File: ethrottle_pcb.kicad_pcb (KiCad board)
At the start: 2 copper layers, 50 parts, among them J1 ATM15-08PA-BM02, K1 1462042-9, U1 LM4040DBZ-5, U2 LM324, U3 LM358_DFN, U4 LM324

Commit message: routes
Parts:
- moved J1 59.0 mm to (141.2, 77.9)
- moved U3 1.13 mm to (114.2, 77.7)
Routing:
- net GND: track 23.2 -> 84.4 mm, vias 20 -> 22
- net Net-(R15-Pad1): track 0.00 -> 9.18 mm
- net Net-(D15-Pad1): track 0.00 -> 5.23 mm
- net 4.5V: track 0.08 -> 4.65 mm
- net Net-(D7-Pad2): track 5.78 -> 9.42 mm
- net Net-(D8-Pad2): track 0.00 -> 2.83 mm
- net Net-(D13-Pad1): track 0.00 -> 2.75 mm
- net Net-(D14-Pad2): track 0.00 -> 2.74 mm
- net Brake: track 0.00 -> 2.10 mm
- net Net-(D2-Pad2): track 0.00 -> 1.80 mm
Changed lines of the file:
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@@
   )
   (footprint "Package_DFN_QFN:DFN-8-1EP_2x2mm_P0.5mm_EP1.05x1.75mm" (layer "F.Cu")
-    (at 115.316 77.6685)
+    (at 114.184 77.736)
     (descr "DFN8 2x2, 0.5P; CASE 506CN (see ON Semiconductor 506CN.PDF)")
     (tags "DFN 0.5")
@@
   )
   (footprint "ATM15-08PA-BM02:ATM1508PABM02" (layer "B.Cu")
-    (at 82.262 79.708 90)
+    (at 141.218 77.928 90)
     (descr "ATM15-08PA-BM02-2")
     (tags "Connector")
@@
   (segment (start 122.936 76.456) (end 120.396 76.456) (width 0.127) (layer "F.Cu") (net 1))
   (segment (start 105.718 82.17) (end 105.718 81.212) (width 0.127) (layer "F.Cu") (net 1))
+  (segment (start 141.218 65.328) (end 140.004 65.328) (width 0.127) (layer "F.Cu") (net 2))
   (segment (start 106.16 83.694) (end 107.496 83.694) (width 0.127) (layer "F.Cu") (net 2))
   (segment (start 102.34 52.054) (end 100.854 52.054) (width 0.127) (layer "F.Cu") (net 2))
@@
   (segment (start 108.208 56.134) (end 108.208 55.63) (width 0.127) (layer "F.Cu") (net 2))
   (segment (start 112.268 81.916) (end 111.506 81.916) (width 0.127) (layer "F.Cu") (net 2))
-  (segment (start 113.3425 78.4185) (end 113.284 78.36) (width 0.127) (layer "F.Cu") (net 2))
+  (segment (start 112.2105 78.486) (end 112.152 78.4275) (width 0.127) (layer "F.Cu") (net 2))
   (segment (start 116.815 58.164) (end 116.84 58.189) (width 0.127) (layer "F.Cu") (net 2))
   (segment (start 109.96 52.054) (end 108.474 52.054) (width 0.127) (layer "F.Cu") (net 2))
   (segment (start 114.554 56.919) (end 115.062 57.427) (width 0.127) (layer "F.Cu") (net 2))
+  (segment (start 140.004 65.328) (end 139.7 65.024) (width 0.127) (layer "F.Cu") (net 2))
   (segment (start 105.156 69.6214) (end 105.156 68.072) (width 0.127) (layer "F.Cu") (net 2))
   (segment (start 111.51 76.2) (end 111.51 76.958) (width 0.127) (layer "F.Cu") (net 2))
   (segment (start 114.554 56.388) (end 114.554 56.919) (width 0.127) (layer "F.Cu") (net 2))
+  (segment (start 129.4065 63.8745) (end 129.54 64.008) (width 0.127) (layer "F.Cu") (net 2))
   (segment (start 116.078 55.395) (end 116.078 54.379) (width 0.127) (layer "F.Cu") (net 2))
   (segment (start 118.872 83.186) (end 119.38 83.694) (width 0.127) (layer "F.Cu") (net 2))
@@
   (segment (start 100.276 68.3744) (end 101.2976 68.3744) (width 0.127) (layer "F.Cu") (net 2))
   (segment (start 100.854 52.054) (end 100.838 52.07) (width 0.127) (layer "F.Cu") (net 2))
+  (segment (start 127.5715 63.8745) (end 129.4065 63.8745) (width 0.127) (layer "F.Cu") (net 2))
   (segment (start 108.474 52.054) (end 108.458 52.07) (width 0.127) (layer "F.Cu") (net 2))
   (segment (start 111.8235 69.39915) (end 111.8235 67.6275) (width 0.127) (layer "F.Cu") (net 2))
-  (segment (start 114.416 78.4185) (end 113.3425 78.4185) (width 0.127) (layer "F.Cu") (net 2))
+  (segment (start 113.284 78.486) (end 112.2105 78.486) (width 0.127) (layer "F.Cu") (net 2))
   (segment (start 111.51 76.958) (end 111.506 76.962) (width 0.127) (layer "F.Cu") (net 2))
   (segment (start 116.078 58.164) (end 116.815 58.164) (width 0.127) (layer "F.Cu") (net 2))
@@
   (via (at 124.206 49.022) (size 0.4) (drill 0.2) (layers "F.Cu" "B.Cu") (net 2))
   (via (at 119.38 83.694) (size 0.4) (drill 0.2) (layers "F.Cu" "B.Cu") (net 2))
-  (via (at 113.284 78.36) (size 0.4) (drill 0.2) (layers "F.Cu" "B.Cu") (net 2))
+  (via (at 112.152 78.4275) (size 0.4) (drill 0.2) (layers "F.Cu" "B.Cu") (net 2))
   (via (at 108.458 52.07) (size 0.4) (drill 0.2) (layers "F.Cu" "B.Cu") (net 2))
+  (via (at 139.7 65.024) (size 0.4) (drill 0.2) (layers "F.Cu" "B.Cu") (net 2))
   (via (at 107.496 83.694) (size 0.4) (drill 0.2) (layers "F.Cu" "B.Cu") (net 2))
   (via (at 112.014 55.88) (size 0.4) (drill 0.2) (layers "F.Cu" "B.Cu") (net 2))
   (via (at 108.989 76.328) (size 0.4) (drill 0.2) (layers "F.Cu" "B.Cu") (net 2))
+  (via (at 129.54 64.008) (size 0.4) (drill 0.2) (layers "F.Cu" "B.Cu") (net 2))
   (via (at 111.506 76.962) (size 0.4) (drill 0.2) (layers "F.Cu" "B.Cu") (net 2))
   (via (at 115.062 81.408) (size 0.4) (drill 0.2) (layers "F.Cu" "B.Cu") (net 2))
@@
   (via (at 105.156 68.072) (size 0.4) (drill 0.2) (layers "F.Cu" "B.Cu") (net 2))
   (via (at 108.204 55.626) (size 0.4) (drill 0.2) (layers "F.Cu" "B.Cu") (net 2))
+  (segment (start 148.618 58.418) (end 130.304 58.418) (width 0.127) (layer "B.Cu") (net 2))
+  (segment (start 126.718 58.418) (end 130.3 58.418) (width 0.127) (layer "B.Cu") (net 2))
+  (segment (start 130.302 58.42) (end 130.302 63.246) (width 0.127) (layer "B.Cu") (net 2))
+  (segment (start 130.3 58.418) (end 130.302 58.42) (width 0.127) (layer "B.Cu") (net 2))
+  (segment (start 126.718 84.838) (end 120.524 84.838) (width 0.127) (layer "B.Cu") (net 2))
+  (segment (start 130.302 63.246) (end 129.54 64.008) (width 0.127) (layer "B.Cu") (net 2))
+  (segment (start 120.524 84.838) (end 119.38 83.694) (width 0.127) (layer "B.Cu") (net 2))
+  (segment (start 148.618 84.838) (end 126.718 84.838) (width 0.127) (layer "B.Cu") (net 2))
+  (segment (start 130.304 58.418) (end 130.302 58.42) (width 0.127) (layer "B.Cu") (net 2))
   (segment (start 116.52 52.888) (end 116.59 52.958) (width 0.127) (layer "F.Cu") (net 3))
+  (segment (start 114.554 55.418) (end 114.554 53.613) (width 0.127) (layer "F.Cu") (net 5))
   (segment (start 100.276 69.3444) (end 100.276 73.602) (width 0.127) (layer "F.Cu") (net 6))
   (segment (start 100.276 73.602) (end 100.334 73.66) (width 0.127) (layer "F.Cu") (net 6))
@@
   (segment (start 120.142 81.916) (end 120.65 81.916) (width 0.127) (layer "B.Cu") (net 8))
   (segment (start 121.666 82.932) (end 122.682 82.932) (width 0.127) (layer "B.Cu") (net 8))
+  (segment (start 106.934 75.694) (end 108.865 75.694) (width 0.127) (layer "F.Cu") (net 9))
+  (segment (start 108.865 75.694) (end 109.501 75.058) (width 0.127) (layer "F.Cu") (net 9))
   (segment (start 122.682 82.428) (end 122.936 82.174) (width 0.127) (layer "F.Cu") (net 10))
   (segment (start 122.936 82.174) (end 122.936 79.756) (width 0.127) (layer "F.Cu") (net 10))
   (segment (start 103.205999 70.276001) (end 103.205999 68.8594) (width 0.127) (layer "F.Cu") (net 13))
+  (segment (start 102.868 75.694) (end 103.632 75.694) (width 0.127) (layer "F.Cu") (net 13))
   (segment (start 100.834 72.648) (end 103.205999 70.276001) (width 0.127) (layer "F.Cu") (net 13))
   (segment (start 100.834 73.66) (end 100.834 72.648) (width 0.127) (layer "F.Cu") (net 13))
+  (segment (start 100.834 73.66) (end 102.868 75.694) (width 0.127) (layer "F.Cu") (net 13))
   (segment (start 105.16 81.078526) (end 105.16 81.154) (width 0.127) (layer "F.Cu") (net 16))
   (segment (start 106.934 79.938) (end 106.734 80.138) (width 0.127) (layer "F.Cu") (net 16))
@@
   (segment (start 106.934 78.994) (end 106.934 79.938) (width 0.127) (layer "F.Cu") (net 16))
   (segment (start 103.632 79.626) (end 105.16 81.154) (width 0.127) (layer "F.Cu") (net 16))
+  (segment (start 112.01 76.2) (end 112.01 76.704) (width 0.127) (layer "F.Cu") (net 17))
+  (segment (start 112.01 76.704) (end 112.792 77.486) (width 0.127) (layer "F.Cu") (net 17))
+  (segment (start 112.792 77.486) (end 113.284 77.486) (width 0.127) (layer "F.Cu") (net 17))
   (segment (start 120.646 80.006) (end 120.396 79.756) (width 0.127) (layer "F.Cu") (net 19))
   (segment (start 120.646 83.186) (end 120.646 80.006) (width 0.127) (layer "F.Cu") (net 19))
   (segment (start 117.09 52.582) (end 119.126 50.546) (width 0.127) (layer "F.Cu") (net 20))
   (segment (start 117.09 52.958) (end 117.09 52.582) (width 0.127) (layer "F.Cu") (net 20))
+  (segment (start 113.156 69.43165) (end 113.1235 69.39915) (width 0.127) (layer "F.Cu") (net 21))
+  (segment (start 113.156 72.136) (end 113.156 69.43165) (width 0.127) (layer "F.Cu") (net 21))
+  (segment (start 117.263 72.852) (end 120.8405 69.2745) (width 0.127) (layer "F.Cu") (net 23))
+  (segment (start 117.094 72.852) (end 117.263 72.852) (width 0.127) (layer "F.Cu") (net 23))
   (segment (start 110.036 75.093) (end 110.036 77.598) (width 0.127) (layer "F.Cu") (net 26))
   (segment (start 110.001 75.058) (end 110.036 75.093) (width 0.127) (layer "F.Cu") (net 26))
+  (segment (start 102.566 73.456) (end 103.856 72.166) (width 0.127) (layer "F.Cu") (net 27))
   (segment (start 102.566 73.66) (end 102.566 73.735474) (width 0.127) (layer "F.Cu") (net 27))
+  (segment (start 102.566 73.66) (end 102.566 73.456) (width 0.127) (layer "F.Cu") (net 27))
+  (segment (start 103.856 72.166) (end 103.856 69.6214) (width 0.127) (layer "F.Cu") (net 27))
   (segment (start 116.5856 70.081) (end 116.611 70.1064) (width 0.127) (layer "F.Cu") (net 28))
   (segment (start 119.126 55.88) (end 119.126 53.846) (width 0.127) (layer "F.Cu") (net 30))
+  (segment (start 109.873499 69.39915) (end 109.873499 72.118501) (width 0.127) (layer "F.Cu") (net 32))
+  (segment (start 109.873499 72.118501) (end 109.856 72.136) (width 0.127) (layer "F.Cu") (net 32))
   (segment (start 117.111 70.1064) (end 117.111 71.865) (width 0.127) (layer "F.Cu") (net 33))
   (segment (start 117.111 71.865) (end 117.094 71.882) (width 0.127) (layer "F.Cu") (net 33))
+  (segment (start 103.206001 63.9826) (end 100.609 61.385599) (width 0.127) (layer "F.Cu") (net 35))
+  (segment (start 100.609 61.385599) (end 100.609 55.88) (width 0.127) (layer "F.Cu") (net 35))
   (zone (net 28) (net_name "+12V") (layer "F.Cu") (name "12V") (hatch edge 0.508)
     (priority 2)

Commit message: update constraints
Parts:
- moved U4 22.8 mm to (128.8, 51.3)
- moved J1 22.6 mm to (118.6, 78.9)
- moved D14 18.6 mm to (129.3, 77.7), turned to 90 degrees
- moved R13 11.0 mm to (111.8, 81.5)
- moved D5 8.36 mm to (109.5, 83.3)
- moved R12 8.36 mm to (112.0, 83.3)
- moved R3 5.67 mm to (114.2, 81.3)
- moved U3 5.67 mm to (116.6, 82.9)
- moved R4 5.34 mm to (110.0, 80.5)
- moved C1 4.94 mm to (101.1, 81.0), turned to -90 degrees
- moved D4 4.83 mm to (106.1, 74.2)
- moved D6 4.83 mm to (107.9, 81.8)
- moved R11 3.71 mm to (106.9, 72.6), turned to 180 degrees
- moved D9 3.07 mm to (123.4, 77.7)
- moved D10 3.07 mm to (126.0, 77.7)
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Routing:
- net GND: track 84.4 -> 40.5 mm, vias 22 -> 16
- net Brake: track 2.10 -> 18.9 mm, vias 0 -> 1
- net Throttle: track 0.00 -> 13.7 mm, vias 0 -> 2
- net 0.5V: track 0.00 -> 11.0 mm
- net Net-(R25-Pad2): track 0.00 -> 7.37 mm
- net Net-(D10-Pad2): track 2.78 -> 9.84 mm
- net Net-(D6-Pad2): track 9.86 -> 3.35 mm, vias 1 -> 0
- net Net-(D7-Pad2): track 9.42 -> 5.02 mm
- net Net-(D9-Pad2): track 3.53 -> 0.00 mm
- net Net-(C1-Pad1): track 5.71 -> 2.54 mm
- net Net-(D8-Pad2): track 2.83 -> 0.00 mm
- net Net-(D13-Pad1): track 2.75 -> 0.00 mm
- net Net-(D14-Pad2): track 2.74 -> 0.00 mm
- net Net-(D15-Pad1): track 5.23 -> 6.88 mm
- net +5V: track 0.00 -> 1.56 mm
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
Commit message: more traces
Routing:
- net Net-(D13-Pad1): track 0.00 -> 37.4 mm, vias 0 -> 4
- net 0.5V: track 11.0 -> 41.5 mm, vias 0 -> 4
- net Net-(C1-Pad1): track 2.54 -> 28.4 mm, vias 0 -> 2
- net Net-(D14-Pad2): track 0.00 -> 25.6 mm
- net 4.5V: track 4.60 -> 27.0 mm, vias 0 -> 3
- net BREF: track 0.00 -> 22.2 mm
- net Net-(C2-Pad1): track 0.00 -> 21.1 mm, vias 0 -> 3
- net Net-(K1-Pad1): track 0.00 -> 17.9 mm, vias 0 -> 2
- net Brake: track 18.9 -> 33.0 mm, vias 1 -> 2
- net Net-(D9-Pad2): track 0.00 -> 12.9 mm
- net Net-(D12-Pad2): track 2.03 -> 12.2 mm
- net Net-(D8-Pad2): track 0.00 -> 6.63 mm
- net Net-(D7-Pad2): track 5.02 -> 8.66 mm
- net GND: track 40.5 -> 42.3 mm, vias 16 -> 17

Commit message: more traces
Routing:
- net +12V: track 0.00 -> 79.6 mm, vias 0 -> 8
- net Net-(D1-Pad2): track 0.00 -> 42.8 mm, vias 0 -> 6
- net Net-(R14-Pad2): track 0.00 -> 42.6 mm, vias 0 -> 2
- net Net-(R18-Pad2): track 0.00 -> 40.4 mm, vias 0 -> 2
- net 4.5V: track 27.0 -> 65.0 mm, vias 3 -> 5
- net Throttle: track 13.7 -> 51.5 mm, vias 2 -> 5
- net Net-(C1-Pad1): track 28.4 -> 65.9 mm, vias 2 -> 4
- net Net-(R15-Pad1): track 9.18 -> 37.8 mm, vias 0 -> 4
- net Net-(D10-Pad2): track 9.84 -> 27.7 mm
- net Brake: track 33.0 -> 49.4 mm, vias 2 -> 3
- net +5V: track 1.58 -> 15.5 mm, vias 0 -> 4
- net Net-(C2-Pad1): track 21.1 -> 33.2 mm
- net Net-(R14-Pad1): track 1.22 -> 12.9 mm
- net Net-(D14-Pad2): track 25.6 -> 29.4 mm
- net GND: track 42.3 -> 40.7 mm, vias 17 -> 16
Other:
- board outline added: 36.8 x 54.6 mm

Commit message: more traces
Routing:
- net TREF: track 0.00 -> 22.8 mm, vias 0 -> 2
- net GND: track 40.7 -> 54.7 mm, vias 16 -> 18
- net Throttle: track 51.5 -> 58.8 mm, vias 5 -> 7
- net 0.5V: track 41.5 -> 47.3 mm
- net Brake: track 49.4 -> 54.0 mm, vias 3 -> 4
- net 4.5V: track 65.0 -> 68.4 mm

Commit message: 0 unconnected
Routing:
- net Net-(R25-Pad2): track 7.37 -> 76.2 mm, vias 0 -> 4
- net GND: track 54.7 -> 100.2 mm, vias 18 -> 24
- net Net-(R23-Pad1): track 0.00 -> 34.4 mm, vias 0 -> 6
- net +5V: track 15.5 -> 45.6 mm, vias 4 -> 8
- net Net-(D13-Pad1): track 37.4 -> 38.6 mm
- net +12V: track 79.6 -> 78.4 mm
- net 4.5V: track 68.4 -> 69.4 mm
- net Net-(C2-Pad1): track 33.2 -> 34.0 mm
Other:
- board size 36.8 x 54.6 mm -> 37.7 x 55.9 mm

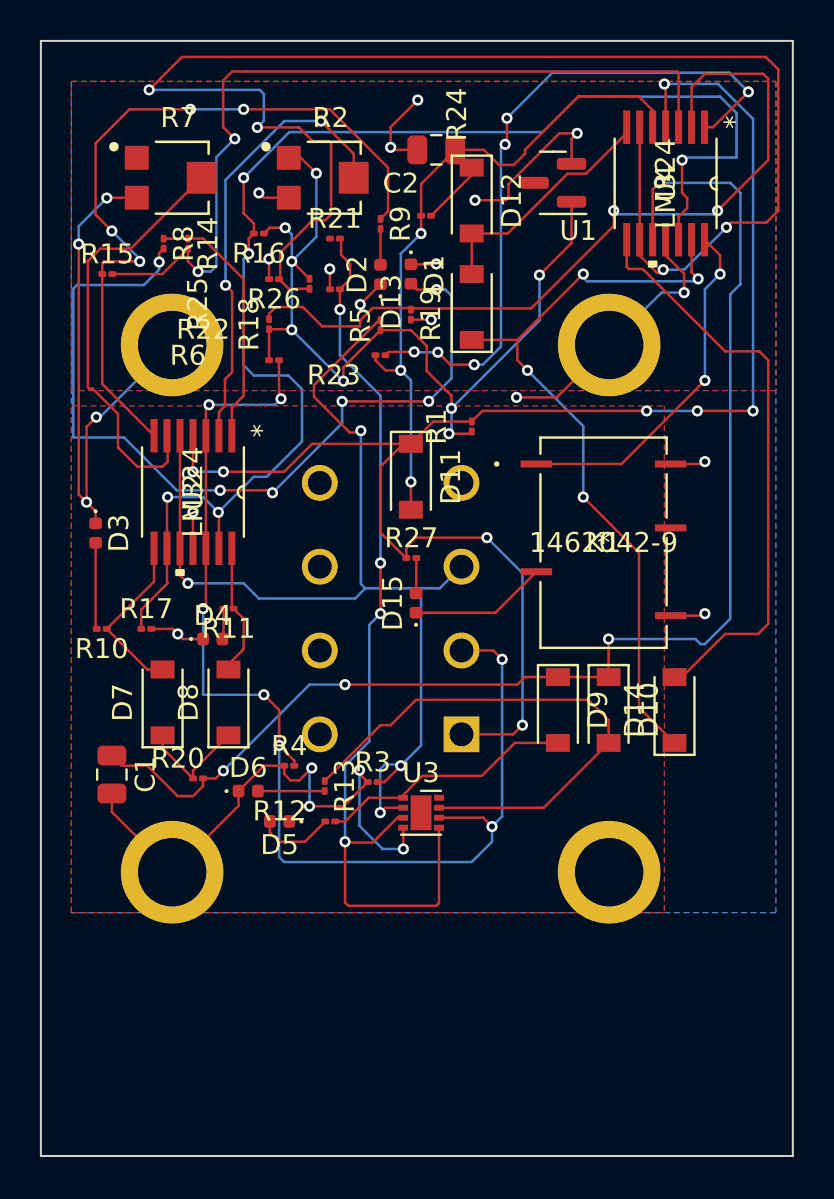
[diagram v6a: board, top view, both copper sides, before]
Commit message: updated schematic, not pcb
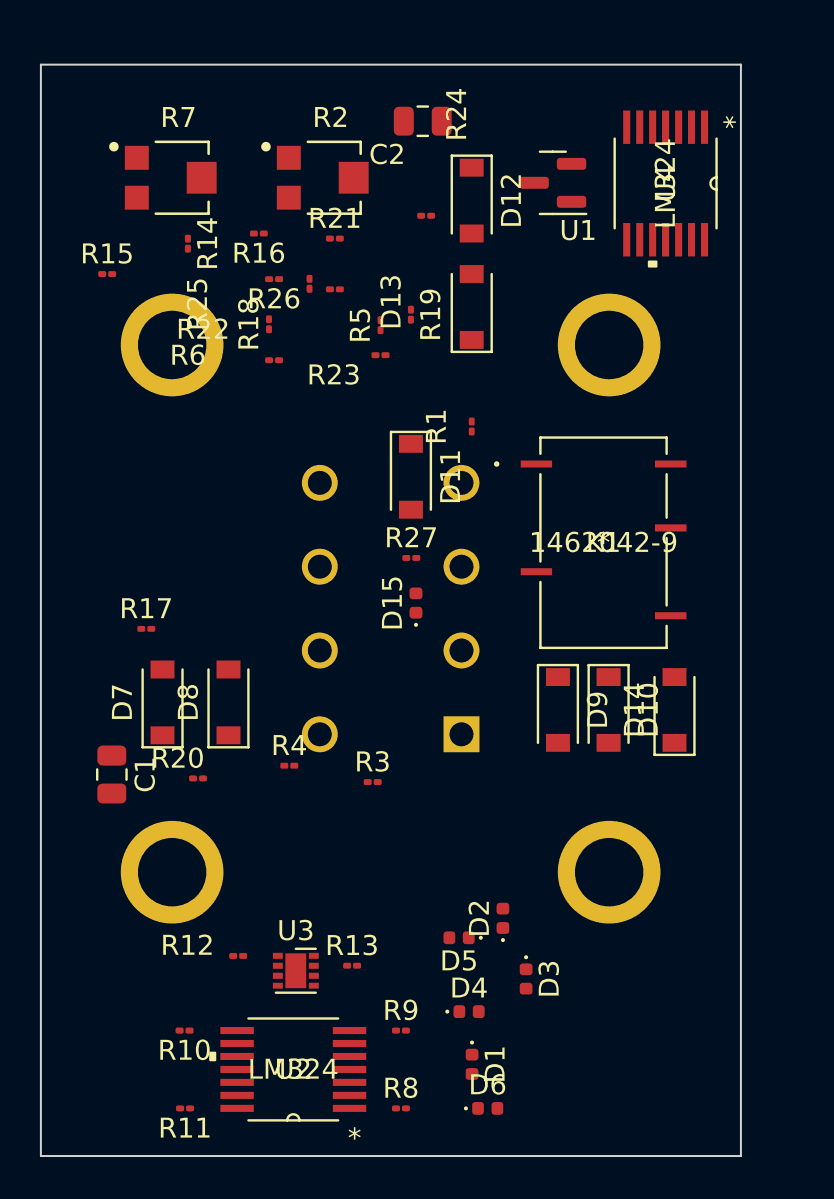
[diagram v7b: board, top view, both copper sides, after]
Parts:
- moved R8 44.9 mm to (115.6, 97.7), turned to 0 degrees
- moved R9 40.4 mm to (115.6, 93.8), turned to 0 degrees
- moved D1 39.7 mm to (119.1, 95.5)
- moved D2 32.8 mm to (120.7, 88.2)
- moved D3 31.1 mm to (121.8, 91.2)
- moved U2 29.4 mm to (110.2, 95.7), turned to 180 degrees
- moved R11 25.1 mm to (104.8, 97.7)
- moved D4 22.7 mm to (119.0, 92.8)
- moved R10 20.6 mm to (104.7, 93.8)
- moved D6 19.9 mm to (119.9, 97.7)
- moved D5 10.7 mm to (118.5, 89.1)
- moved U3 10.1 mm to (110.3, 90.8)
- moved R13 9.11 mm to (113.1, 90.5), turned to 0 degrees
- moved R12 8.17 mm to (107.4, 90.0)
- moved C2 1.59 mm to (116.7, 48.2)
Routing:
- net GND: track 100.2 -> 0.00 mm, vias 24 -> 0
- net +12V: track 78.4 -> 0.00 mm, vias 8 -> 0
- net Net-(R25-Pad2): track 76.2 -> 0.00 mm, vias 4 -> 0
- net 4.5V: track 69.4 -> 0.00 mm, vias 5 -> 0
- net Net-(C1-Pad1): track 65.9 -> 0.00 mm, vias 4 -> 0
- net Throttle: track 58.8 -> 0.00 mm, vias 7 -> 0
- net Brake: track 54.0 -> 0.00 mm, vias 4 -> 0
- net 0.5V: track 47.3 -> 0.00 mm, vias 4 -> 0
- net +5V: track 45.6 -> 0.00 mm, vias 8 -> 0
- net Net-(D1-Pad2): track 42.8 -> 0.00 mm, vias 6 -> 0
- net Net-(R14-Pad2): track 42.4 -> 0.00 mm, vias 2 -> 0
- net Net-(R18-Pad2): track 40.4 -> 0.00 mm, vias 2 -> 0
- net Net-(D13-Pad1): track 38.6 -> 0.00 mm, vias 4 -> 0
- net Net-(R15-Pad1): track 37.8 -> 0.00 mm, vias 4 -> 0
- net Net-(R23-Pad1): track 34.4 -> 0.00 mm, vias 6 -> 0
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- removed copper zone on F.Cu, net +12V
- removed copper zone on F.Cu, net +5V
- removed copper zone on B.Cu, net GND
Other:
- board size 37.7 x 55.9 mm -> 35.1 x 54.7 mm

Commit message: updates
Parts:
- removed K1: 1462042-9, ul_1462042-9:1462042-9
- removed the R1 at (119.1, 63.5)
- added C1: 100nF, Capacitor_SMD:C_0201_0603Metric, F.Cu at (172.6, 59.4)
- added C3: 100nF, Capacitor_SMD:C_0201_0603Metric, F.Cu at (141.5, 76.0)
- added C4: 100nF, Capacitor_SMD:C_0201_0603Metric, F.Cu at (169.5, 65.2)
- added D16: CGRM4007-G, Diode_SMD:D_SOD-123, F.Cu at (137.4, 76.8)
- added Q1: ZXTR2105F-7, ZXTR2105F-7:ZXTR2105F-7, F.Cu at (165.1, 59.6)
- U1: value LM4040DBZ-5 -> MCP6004; footprint Package_TO_SOT_SMD:SOT-23 -> MCP6004T-I_ST:SOP65P640X120-14N
- U2: value LM324 -> MCP6004; footprint LM324PWR:LM324PWR -> MCP6004T-I_ST:SOP65P640X120-14N
- U3: value LM358_DFN -> MCP6004; footprint Package_DFN_QFN:DFN-8-1EP_2x2mm_P0.5mm_EP1.05x1.75mm -> MCP6004T-I_ST:SOP65P640X120-14N
- U4: value LM324 -> UB2-5NUN; footprint LM324PWR:LM324PWR -> UB2-5NUN:UB2-5NUN
- moved U3 74.1 mm to (175.4, 55.4)
- moved U2 58.3 mm to (164.2, 73.6), turned to 0 degrees
- moved U1 44.0 mm to (164.2, 67.4), turned to 0 degrees
- moved U4 22.4 mm to (143.5, 68.2), turned to 0 degrees
- renumbered C1 to C2, C2 to C5, R2 to R1, R11 to R10, R12 to R11, R13 to R12, R14 to R13, R15 to R14, R16 to R15, R17 to R16, R18 to R17, R19 to R18, R20 to R19, R3 to R2, R21 to R20, R22 to R21, R23 to R22, R24 to R23, R25 to R24, R26 to R25, R27 to R26, R4 to R3, R5 to R4, R6 to R5, R7 to R6, R8 to R7, R9 to R8, R10 to R9
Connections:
- C2 pad 1: Net-(C1-Pad1) -> Net-(C2-Pad1)
- C5 pad 1: Net-(C2-Pad1) -> Net-(C5-Pad1)
- D10 pad 1: Net-(C1-Pad1) -> Net-(C2-Pad1)
- D11 pad 2: Net-(C2-Pad1) -> Net-(C5-Pad1)
- D15 pad 1: Net-(D15-Pad1) -> GND
- D9 pad 1: Net-(C1-Pad1) -> Net-(C2-Pad1)
- J1 pad 5: unconnected-(J1-Pad5) -> Output
- R13 pad 1: Net-(R14-Pad1) -> Net-(R13-Pad1)
- R13 pad 2: Net-(R14-Pad2) -> Net-(R13-Pad2)
- R14 pad 1: Net-(R15-Pad1) -> Net-(R14-Pad1)
- R14 pad 2: Net-(R14-Pad2) -> Net-(R13-Pad2)
- R17 pad 2: Net-(R18-Pad2) -> Net-(R17-Pad2)
- R18 pad 1: Net-(R18-Pad2) -> Net-(R17-Pad2)
- R19 pad 2: Net-(C1-Pad1) -> Net-(C2-Pad1)
- R22 pad 1: Net-(R23-Pad1) -> Net-(R22-Pad1)
- R22 pad 2: Net-(C2-Pad1) -> Net-(C5-Pad1)
- R23 pad 2: Net-(C2-Pad1) -> Net-(C5-Pad1)
- R24 pad 2: Net-(R25-Pad2) -> Net-(R24-Pad2)
- R25 pad 1: Net-(R25-Pad2) -> Net-(R24-Pad2)
- R7 pad 1: Net-(R14-Pad1) -> Net-(R13-Pad1)
- R8 pad 1: Net-(R15-Pad1) -> Net-(R14-Pad1)
- U1 pad 1: +5V -> Net-(R13-Pad1)
- U1 pad 2: GND -> TREF
- U1 pad 3: (no net) -> Throttle
- U2 pad 1: Net-(R14-Pad1) -> Net-(D9-Pad2)
- U2 pad 10: Brake -> Net-(C2-Pad1)
- U2 pad 12: Throttle -> 4.5V
- U2 pad 13: 4.5V -> Net-(D13-Pad1)
- U2 pad 14: Net-(D8-Pad2) -> Net-(D16-Pad1)
- U2 pad 2: TREF -> Brake
- U2 pad 3: Throttle -> 0.5V
- U2 pad 4: +12V -> +5V
- U2 pad 5: Brake -> 0.5V
- U2 pad 6: BREF -> Throttle
- U2 pad 7: Net-(R15-Pad1) -> Net-(D10-Pad2)
- U2 pad 8: Net-(D7-Pad2) -> Net-(D14-Pad2)
- U2 pad 9: 4.5V -> Net-(R24-Pad2)
- U3 pad 1: Net-(D9-Pad2) -> Net-(R22-Pad1)
- U3 pad 2: Brake -> Net-(R17-Pad2)
- U3 pad 3: 0.5V -> Net-(R13-Pad2)
- U3 pad 4: GND -> +5V
- U3 pad 5: 0.5V -> Net-(C5-Pad1)
- U3 pad 6: Throttle -> Net-(R24-Pad2)
- U3 pad 7: Net-(D10-Pad2) -> Net-(D12-Pad2)
- U3 pad 8: +12V -> (no net)
- U3 pad 9: unconnected-(U3-Pad9) -> (no net)
- U4 pad 1: Net-(R23-Pad1) -> Net-(D16-Pad1)
- U4 pad 2: Net-(R18-Pad2) -> Output
- U4 pad 3: Net-(R14-Pad2) -> Output
- U4 pad 5: Net-(C2-Pad1) -> +12V
- U4 pad 6: Net-(R25-Pad2) -> Output
- U4 pad 7: Net-(D12-Pad2) -> Output
- U4 pad 8: Net-(D14-Pad2) -> GND
